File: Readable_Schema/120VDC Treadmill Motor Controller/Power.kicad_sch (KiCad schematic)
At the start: 3 parts, among them J1 Conn_01x02_Pin

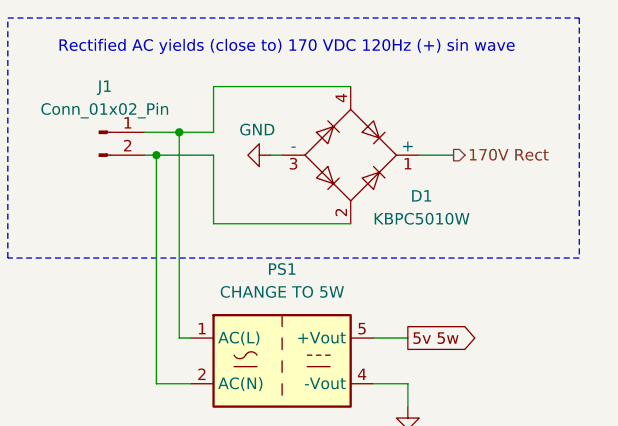
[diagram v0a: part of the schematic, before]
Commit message: I cant for the life of me get the current sensing to actually properly scale with current, I treid 5 different sim models and right now the DA is the best but doesnt start showing anything till around 19amps which kind of defeats the purpose
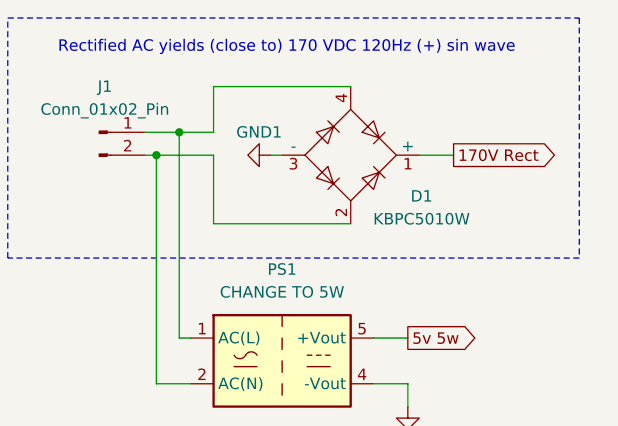
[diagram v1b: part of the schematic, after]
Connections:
- net GND: no longer D1.3 (-)
- new net GND1: D1.3 (-)
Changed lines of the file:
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@@
+		)
+	)
+	(global_label "170V Rect"
+		(shape output)
+		(at 157.48 82.55 0)
+		(fields_autoplaced yes)
+		(effects
+			(font
+				(size 1.27 1.27)
+			)
+			(justify left)
+		)
+		(property "Intersheetrefs" "${INTERSHEET_REFS}"
+			(at 170.3228 82.55 0)
+			(effects
+				(font
+					(size 1.27 1.27)
+				)
+				(justify left)
+				(hide yes)
+			)
 		)
 	)
@@
 				(hide yes)
 			)
-		)
-	)
-	(hierarchical_label "170V Rect"
-		(shape output)
-		(at 157.48 82.55 0)
-		(effects
-			(font
-				(size 1.27 1.27)
-			)
-			(justify left)
 		)
 	)
@@
 	)
 	(symbol
-		(lib_id "power:GND")
+		(lib_id "power:GND1")
 		(at 137.16 82.55 270)
 		(unit 1)
@@
 			)
 		)
-		(property "Value" "GND"
-			(at 137.668 79.756 90)
+		(property "Value" "GND1"
+			(at 138.43 80.01 90)
 			(effects
 				(font
@@
 			)
 		)
-		(property "Description" "Power symbol creates a global label with name \"GND\" , ground"
+		(property "Description" "Power symbol creates a global label with name \"GND1\" , ground"
 			(at 137.16 82.55 0)
 			(effects

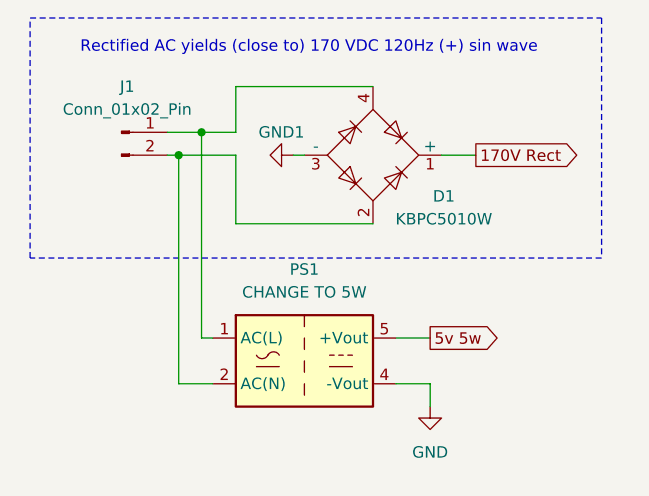
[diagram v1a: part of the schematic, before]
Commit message: Continuing to update footprints, did some follow up math on low pass filter for adc voltage coming out of current sense system
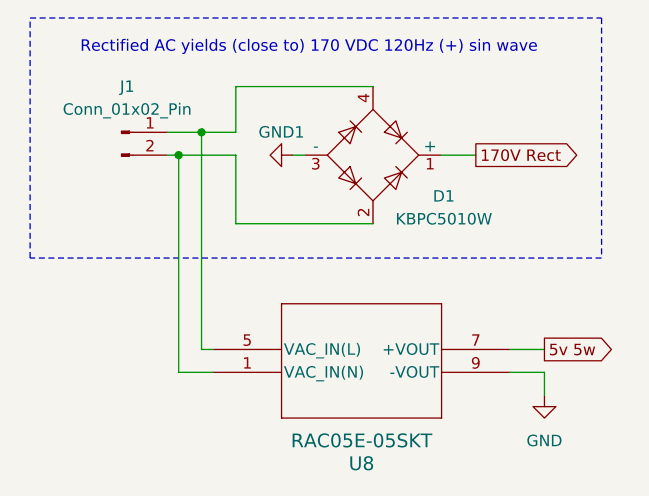
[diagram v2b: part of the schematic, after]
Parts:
- removed PS1: CHANGE TO 5W, symbol Converter_ACDC:RAC05-24SK
- added U8: RAC05E-05SKT, Treadmill_Feet:RAC05E-KT_RCP, symbol Treadmill_Comp:RAC05E-05SKT
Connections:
- net 5v 5w: now also U8.7 (+VOUT)
- net GND: now also U8.9 (-VOUT)
- net at D1.4, J1.1 (Pin_1): now also U8.5 (VAC_IN(L))
- net at D1.2, J1.2 (Pin_2): now also U8.1 (VAC_IN(N))
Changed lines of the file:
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@@
 	(wire
 		(pts
-			(xy 152.4 110.49) (xy 152.4 107.95)
-		)
-		(stroke
-			(width 0)
-			(type default)
-		)
-	)
-	(wire
-		(pts
-			(xy 148.59 107.95) (xy 152.4 107.95)
+			(xy 165.1 109.22) (xy 165.1 106.68)
+		)
+		(stroke
+			(width 0)
+			(type default)
+		)
+	)
+	(wire
+		(pts
+			(xy 161.29 106.68) (xy 165.1 106.68)
 		)
 		(stroke
@@
 	(wire
 		(pts
-			(xy 124.46 82.55) (xy 124.46 107.95)
-		)
-		(stroke
-			(width 0)
-			(type default)
-		)
-	)
-	(wire
-		(pts
-			(xy 128.27 107.95) (xy 124.46 107.95)
+			(xy 124.46 82.55) (xy 124.46 106.68)
+		)
+		(stroke
+			(width 0)
+			(type default)
+		)
+	)
+	(wire
+		(pts
+			(xy 128.27 106.68) (xy 124.46 106.68)
 		)
 		(stroke
@@
 	(wire
 		(pts
-			(xy 128.27 102.87) (xy 127 102.87)
+			(xy 128.27 104.14) (xy 127 104.14)
 		)
 		(stroke
@@
 	(wire
 		(pts
-			(xy 148.59 102.87) (xy 152.4 102.87)
+			(xy 161.29 104.14) (xy 165.1 104.14)
 		)
 		(stroke
@@
 	(wire
 		(pts
-			(xy 127 80.01) (xy 127 102.87)
+			(xy 127 80.01) (xy 127 104.14)
 		)
 		(stroke
@@
 	(global_label "5v 5w"
 		(shape output)
-		(at 152.4 102.87 0)
+		(at 165.1 104.14 0)
 		(fields_autoplaced yes)
 		(effects
@@
 		)
 		(property "Intersheetrefs" "${INTERSHEET_REFS}"
-			(at 161.0699 102.87 0)
+			(at 173.7699 104.14 0)
 			(effects
 				(font
@@
 	(symbol
 		(lib_id "power:GND")
-		(at 152.4 110.49 0)
+		(at 165.1 109.22 0)
 		(unit 1)
 		(exclude_from_sim no)
@@
 		(fields_autoplaced yes)
 		(property "Reference" "#PWR01"
-			(at 152.4 116.84 0)
+			(at 165.1 115.57 0)
 			(effects
 				(font
@@
 		)
 		(property "Value" "GND"
-			(at 152.4 115.57 0)
+			(at 165.1 114.3 0)
 			(effects
 				(font
@@
 		)
 		(property "Footprint" ""
-			(at 152.4 110.49 0)
+			(at 165.1 109.22 0)
 			(effects
 				(font
@@
 		)
 		(property "Datasheet" ""
-			(at 152.4 110.49 0)
+			(at 165.1 109.22 0)
 			(effects
 				(font
@@
 		)
 		(property "Description" "Power symbol creates a global label with name \"GND\" , ground"
-			(at 152.4 110.49 0)
+			(at 165.1 109.22 0)
 			(effects
 				(font
@@
 				(path "/319bc5c0-2dd5-4df3-a34b-9170833ebccd/1fa0373b-ff98-4bf0-acad-d32450f2dcd0"
 					(reference "#PWR01")
+					(unit 1)
+				)
+			)
+		)
+	)
+	(symbol
+		(lib_id "Treadmill_Comp:RAC05E-05SKT")
+		(at 119.38 106.68 0)
+		(mirror x)
+		(unit 1)
+		(exclude_from_sim no)
+		(in_bom yes)
+		(on_board yes)
+		(dnp no)
+		(property "Reference" "U8"
+			(at 144.78 116.84 0)
+			(effects
+				(font
+					(size 1.524 1.524)
+				)
+			)
+		)
+		(property "Value" "RAC05E-05SKT"
+			(at 144.78 114.3 0)
+			(effects
+				(font
+					(size 1.524 1.524)
+				)
+			)
+		)
+		(property "Footprint" "Treadmill_Feet:RAC05E-KT_RCP"
+			(at 128.27 106.68 0)
+			(effects
+				(font
+					(size 1.27 1.27)
+					(italic yes)
+				)
+				(hide yes)
+			)
+		)
+		(property "Datasheet" "https://recom-power.com/pdf/Powerline_AC-DC/RAC05E-KT.pdf"
+			(at 128.27 106.68 0)
+			(effects
+				(font
+					(size 1.27 1.27)
+					(italic yes)
+				)
+				(hide yes)
+			)
+		)
+		(property "Description" ""
+			(at 119.38 106.68 0)
+			(effects
+				(font
+					(size 1.27 1.27)
+				)
+				(hide yes)
+			)
+		)
+		(pin "9"
+		)
+		(pin "5"
+		)
+		(pin "7"
+		)
+		(pin "1"
+		)
+		(instances
+			(project ""
+				(path "/319bc5c0-2dd5-4df3-a34b-9170833ebccd/1fa0373b-ff98-4bf0-acad-d32450f2dcd0"
+					(reference "U8")
 					(unit 1)
 				)
@@
 					(unit 1)
 				)
-			)
-		)
-	)
-	(symbol
-		(lib_id "Converter_ACDC:RAC05-24SK")
-		(at 138.43 105.41 0)
-		(unit 1)
-		(exclude_from_sim no)
-		(in_bom yes)
-		(on_board yes)
-		(dnp no)
-		(fields_autoplaced yes)
-		(property "Reference" "PS1"
-			(at 138.43 95.25 0)
-			(effects
-				(font
-					(size 1.27 1.27)
-				)
-			)
-		)
-		(property "Value" "CHANGE TO 5W"
-			(at 138.43 97.79 0)
-			(effects
-				(font
-					(size 1.27 1.27)
-					(thickness 0.1588)
-				)
-			)
-		)
-		(property "Footprint" ""
-			(at 138.43 114.3 0)
-			(effects
-				(font
-					(size 1.27 1.27)
-				)
-				(hide yes)
-			)
-		)
-		(property "Datasheet" "https://www.meanwell.com/upload/pdf/IRM-01/IRM-01-spec.pdf"
-			(at 135.89 97.79 0)
-			(effects
-				(font
-					(size 1.27 1.27)
-				)
-				(hide yes)
-			)
-		)
-		(property "Description" "1W 5v Ac Dc Power Supply"
-			(at 138.43 105.41 0)
-			(effects
-				(font
-					(size 1.27 1.27)
-				)
-				(hide yes)
-			)
-		)
-		(pin "1"
-		)
-		(pin "2"
-		)
-		(pin "4"
-		)
-		(pin "3"
-		)
-		(pin "5"
-		)
-		(instances
-			(project ""
-				(path "/319bc5c0-2dd5-4df3-a34b-9170833ebccd/1fa0373b-ff98-4bf0-acad-d32450f2dcd0"
-					(reference "PS1")
-					(unit 1)
-				)

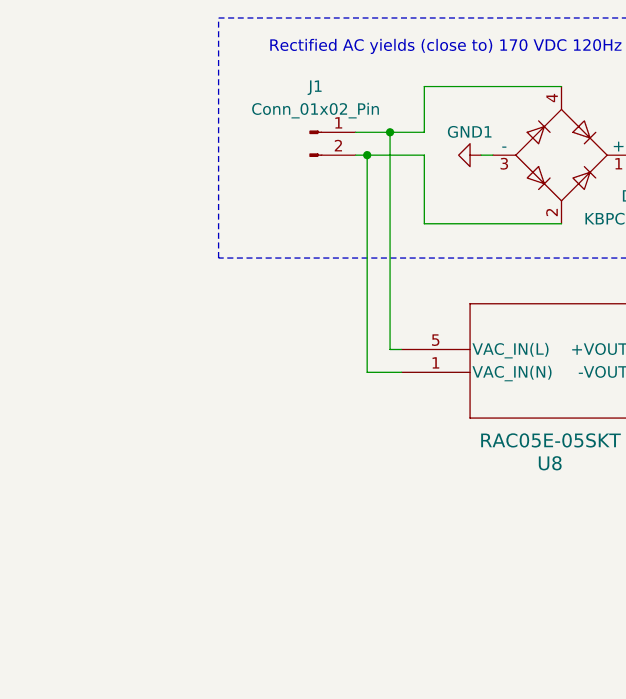
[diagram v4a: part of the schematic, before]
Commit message: started working on the e_stop circuit. Basically just using a relay to shut off all power to the system, including both the mcu and the 170 DC 120HZ.
-Need to finish the E_stop subcircuit
-Still need to start wrapping up the brake resistor subcircuit
-input capacitor sizing
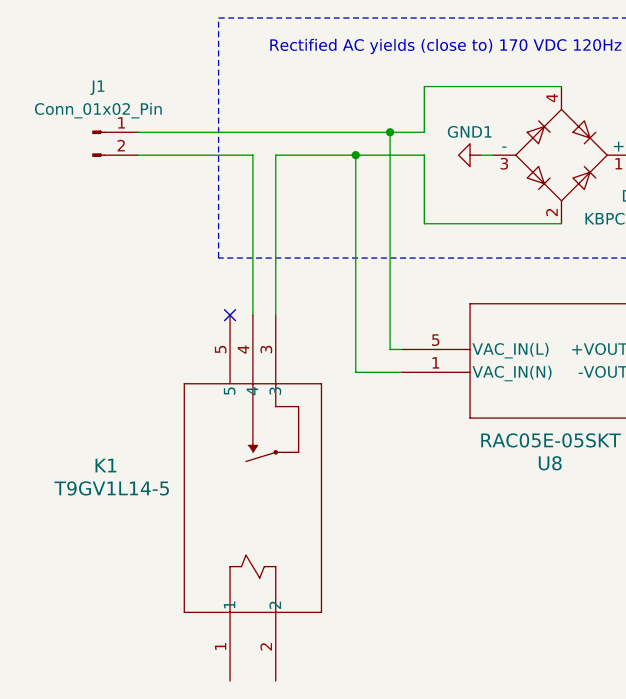
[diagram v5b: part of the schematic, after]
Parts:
- added K1: T9GV1L14-5, T9GV1L14-5_TEC, symbol Treadmill_Comp:T9GV1L14-5
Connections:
- net at D1.2, U8.1 (VAC_IN(N)): now also K1.3; no longer J1.2 (Pin_2)
- new net: J1.2 (Pin_2), K1.4
- no-connect marks 0 -> 1
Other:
- moved on the sheet: J1
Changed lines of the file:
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@@
 	)
 	(junction
-		(at 124.46 82.55)
+		(at 123.19 82.55)
 		(diameter 0)
 		(color 0 0 0 0)
 	)
+	(no_connect
+		(at 109.22 100.33)
+	)
 	(wire
 		(pts
@@
 	(wire
 		(pts
-			(xy 124.46 82.55) (xy 130.81 82.55)
-		)
-		(stroke
-			(width 0)
-			(type default)
-		)
-	)
-	(wire
-		(pts
-			(xy 124.46 82.55) (xy 124.46 106.68)
-		)
-		(stroke
-			(width 0)
-			(type default)
-		)
-	)
-	(wire
-		(pts
-			(xy 128.27 106.68) (xy 124.46 106.68)
-		)
-		(stroke
-			(width 0)
-			(type default)
-		)
-	)
-	(wire
-		(pts
-			(xy 123.19 80.01) (xy 127 80.01)
+			(xy 123.19 82.55) (xy 123.19 106.68)
+		)
+		(stroke
+			(width 0)
+			(type default)
+		)
+	)
+	(wire
+		(pts
+			(xy 128.27 106.68) (xy 123.19 106.68)
+		)
+		(stroke
+			(width 0)
+			(type default)
+		)
+	)
+	(wire
+		(pts
+			(xy 111.76 100.33) (xy 111.76 82.55)
+		)
+		(stroke
+			(width 0)
+			(type default)
+		)
+	)
+	(wire
+		(pts
+			(xy 99.06 80.01) (xy 127 80.01)
 		)
 		(stroke
@@
 	(wire
 		(pts
-			(xy 123.19 82.55) (xy 124.46 82.55)
+			(xy 99.06 82.55) (xy 111.76 82.55)
 		)
 		(stroke
@@
 	(wire
 		(pts
+			(xy 123.19 82.55) (xy 130.81 82.55)
+		)
+		(stroke
+			(width 0)
+			(type default)
+		)
+	)
+	(wire
+		(pts
 			(xy 130.81 74.93) (xy 146.05 74.93)
 		)
@@
 	(wire
 		(pts
+			(xy 114.3 100.33) (xy 114.3 82.55)
+		)
+		(stroke
+			(width 0)
+			(type default)
+		)
+	)
+	(wire
+		(pts
 			(xy 130.81 90.17) (xy 146.05 90.17)
 		)
@@
 		(pts
 			(xy 127 80.01) (xy 127 104.14)
+		)
+		(stroke
+			(width 0)
+			(type default)
+		)
+	)
+	(wire
+		(pts
+			(xy 114.3 82.55) (xy 123.19 82.55)
 		)
 		(stroke
@@
 	)
 	(symbol
+		(lib_id "Treadmill_Comp:T9GV1L14-5")
+		(at 109.22 140.97 90)
+		(unit 1)
+		(exclude_from_sim no)
+		(in_bom yes)
+		(on_board yes)
+		(dnp no)
+		(property "Reference" "K1"
+			(at 96.774 117.094 90)
+			(effects
+				(font
+					(size 1.524 1.524)
+				)
+				(justify left)
+			)
+		)
+		(property "Value" "T9GV1L14-5"
+			(at 102.616 119.634 90)
+			(effects
+				(font
+					(size 1.524 1.524)
+				)
+				(justify left)
+			)
+		)
+		(property "Footprint" "T9GV1L14-5_TEC"
+			(at 109.22 140.97 0)
+			(effects
+				(font
+					(size 1.27 1.27)
+					(italic yes)
+				)
+				(hide yes)
+			)
+		)
+		(property "Datasheet" "https://www.te.com/commerce/DocumentDelivery/DDEController?Action=srchrtrv&DocNm=1-1773924-8_PB_30A_PCB_RelayT9G&DocType=Data+Sheet&DocLang=English&PartCntxt=1558661-1&DocFormat=pdf"
+			(at 109.22 140.97 0)
+			(effects
+				(font
+					(size 1.27 1.27)
+					(italic yes)
+				)
+				(hide yes)
+			)
+		)
+		(property "Description" ""
+			(at 109.22 140.97 0)
+			(effects
+				(font
+					(size 1.27 1.27)
+				)
+				(hide yes)
+			)
+		)
+		(pin "4"
+		)
+		(pin "1"
+		)
+		(pin "2"
+		)
+		(pin "5"
+		)
+		(pin "3"
+		)
+		(instances
+			(project ""
+				(path "/319bc5c0-2dd5-4df3-a34b-9170833ebccd/1fa0373b-ff98-4bf0-acad-d32450f2dcd0"
+					(reference "K1")
+					(unit 1)
+				)
+			)
+		)
+	)
+	(symbol
 		(lib_id "Treadmill_Comp:RAC05E-05SKT")
 		(at 119.38 106.68 0)
@@
 	(symbol
 		(lib_id "Connector:Conn_01x02_Pin")
-		(at 118.11 80.01 0)
+		(at 93.98 80.01 0)
 		(unit 1)
 		(exclude_from_sim no)
@@
 		(fields_autoplaced yes)
 		(property "Reference" "J1"
-			(at 118.745 74.93 0)
+			(at 94.615 74.93 0)
 			(effects
 				(font
@@
 		)
 		(property "Value" "Conn_01x02_Pin"
-			(at 118.745 77.47 0)
+			(at 94.615 77.47 0)
 			(effects
 				(font
@@
 		)
 		(property "Footprint" ""
-			(at 118.11 80.01 0)
+			(at 93.98 80.01 0)
 			(effects
 				(font
@@
 		)
 		(property "Datasheet" "~"
-			(at 118.11 80.01 0)
+			(at 93.98 80.01 0)
 			(effects
 				(font
@@
 		)
 		(property "Description" "Generic connector, single row, 01x02, script generated"
-			(at 118.11 80.01 0)
-			(effects
-				(font
+			(at 93.98 80.01 0)
+			(effects
+				(font
